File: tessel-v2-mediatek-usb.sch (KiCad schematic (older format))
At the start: 49 parts, among them J901 USB_A_2_stack, J902 USB_A_2_stack, U201 MT7620N, U901 AIC1528-0PSTR, U902 AIC1528-0PSTR, U903 FE1.1, X901 12MHz

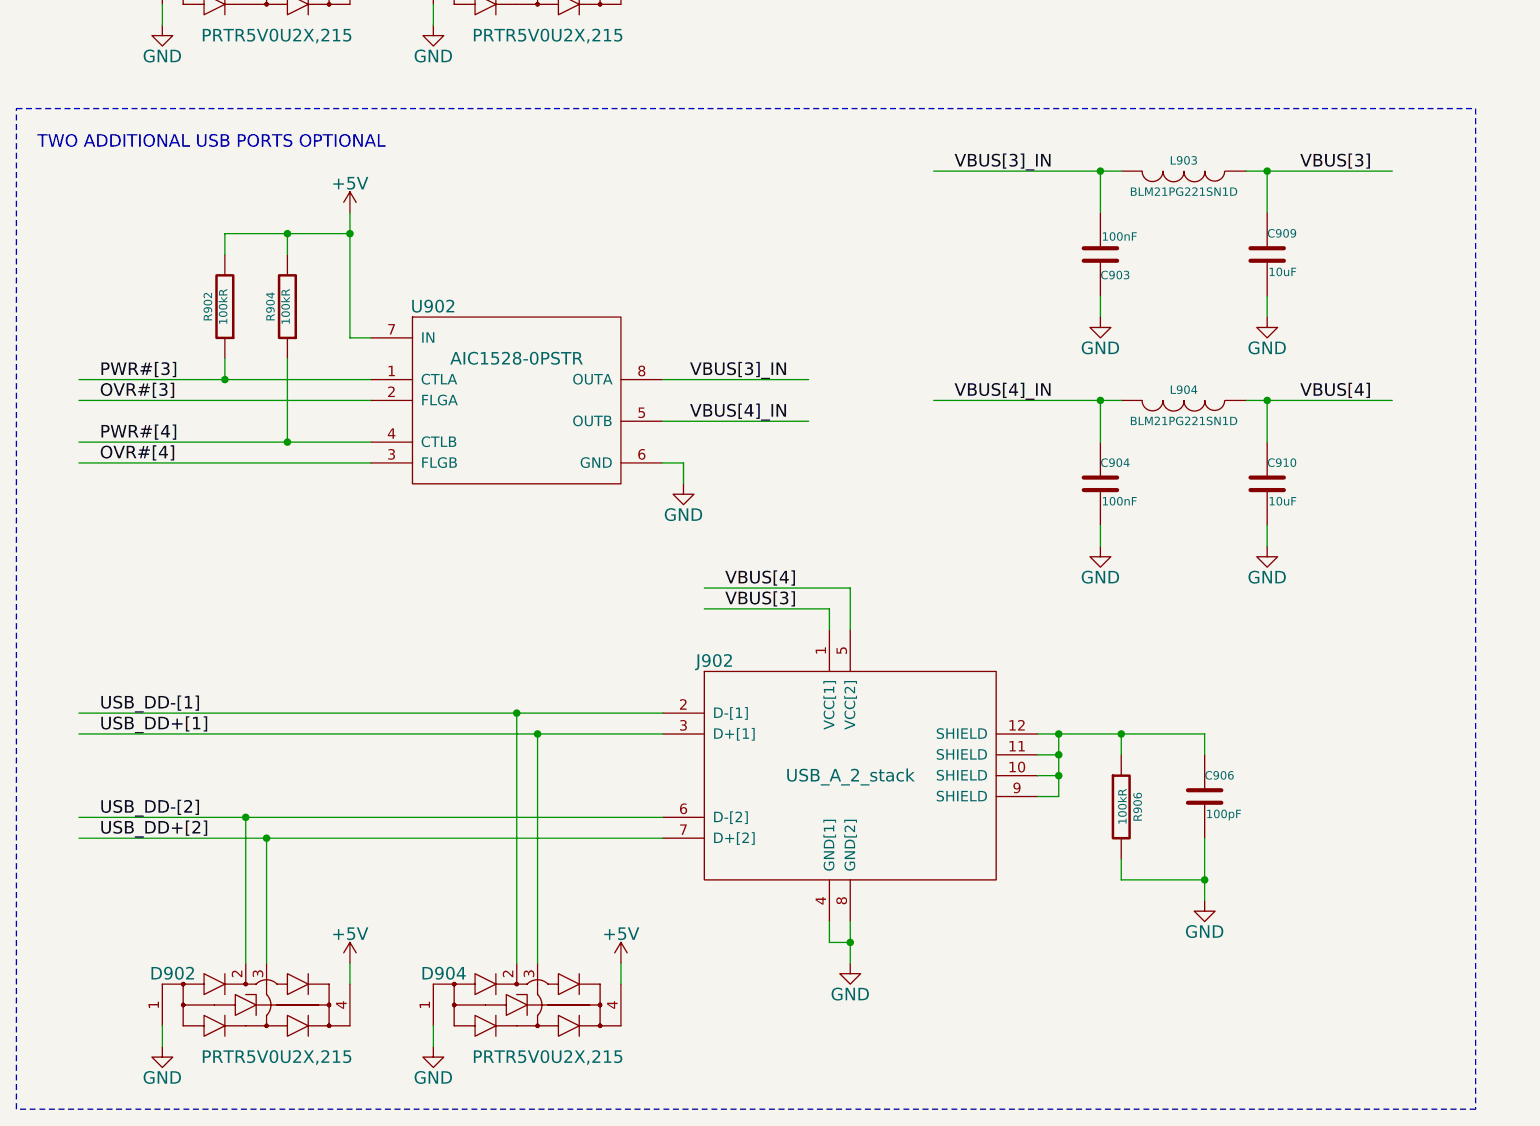
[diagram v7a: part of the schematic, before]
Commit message: removed second set of usb ports
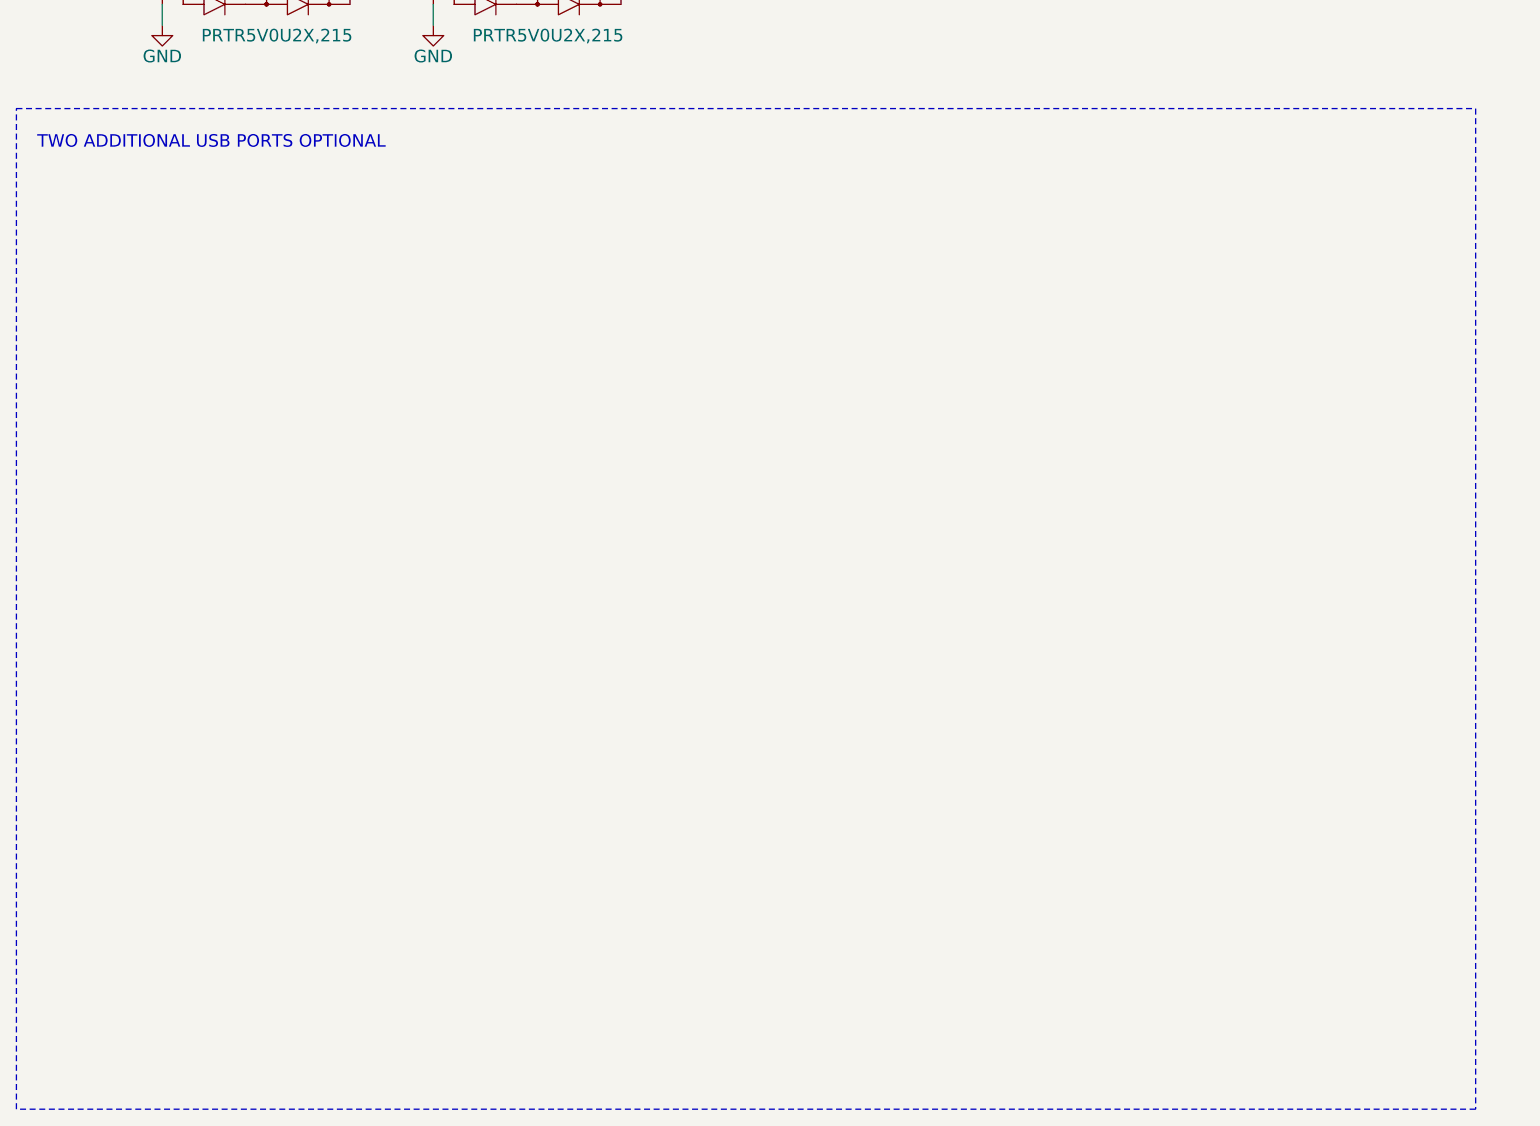
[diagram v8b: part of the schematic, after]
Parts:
- removed C903, C904: 100nF, tm-kicad-lib:SMD-0402-C, symbol C
- removed C906: 100pF, tm-kicad-lib:SMD-0402-C, symbol C
- removed C909, C910: 10uF, SMD_Packages:SMD-0805, symbol C
- removed D902, D904: PRTR5V0U2X,215, tm-kicad-lib:PRTR5V0U2X,215, symbol PRTR5V0U2X,215
- removed J902: USB_A_2_stack, tm-kicad-lib:USB-double-xx-UAF-28, symbol USB_A_2_stack
- removed L903, L904: BLM21PG221SN1D, SMD_Packages:SMD-0805, symbol INDUCTOR
- removed R902, R904, R906: 100kR, tm-kicad-lib:SMD-0402-R, symbol R
- removed U902: AIC1528-0PSTR, tm-kicad-lib:SOP-8, symbol AIC1528-0PSTR
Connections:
- net labels removed: VBUS[3], VBUS[3]_IN, VBUS[4], VBUS[4]_IN
- wire segments 202 -> 146
